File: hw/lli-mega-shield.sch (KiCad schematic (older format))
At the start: 6 parts

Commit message: Some schematics
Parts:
- added C? (x2): 1uF, symbol C
- added R? (x2): 75, symbol R
- added U? (x4): LM35, symbol LM35
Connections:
- wire segments 12 -> 26
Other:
- note added: "Battery Sensor"
- note added: "Temperature Sensors"
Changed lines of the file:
@@
-EESchema Schematic File Version 2  date fre 07 sep 2012 19:08:03 CEST
+EESchema Schematic File Version 2  date fre 07 sep 2012 20:49:57 CEST
 LIBS:power
 LIBS:device
@@
 Comment4 ""
 $EndDescr
+Text Notes 3300 4800 0    60   Italic 12
+Battery Sensor
+Text Notes 900  2800 0    60   Italic 12
+Temperature Sensors
+$Comp
+L LM35 U?
+U 1 1 504A41AE
+P 1500 4500
+F 0 "U?" H 1500 4650 60  0000 C CNN
+F 1 "LM35" H 1650 4250 60  0000 C CNN
+	1    1500 4500
+	1    0    0    -1
+$EndComp
+$Comp
+L R R?
+U 1 1 504A41AD
+P 2150 4800
+F 0 "R?" V 2230 4800 50  0000 C CNN
+F 1 "75" V 2150 4800 50  0000 C CNN
+	1    2150 4800
+	1    0    0    -1
+$EndComp
+$Comp
+L C C?
+U 1 1 504A41AC
+P 2150 5300
+F 0 "C?" H 2200 5400 50  0000 L CNN
+F 1 "1uF" H 2200 5200 50  0000 L CNN
+	1    2150 5300
+	1    0    0    -1
+$EndComp
+$Comp
+L GND #PWR?
+U 1 1 504A41AB
+P 1500 5100
+F 0 "#PWR?" H 1500 5100 30  0001 C CNN
+F 1 "GND" H 1500 5030 30  0001 C CNN
+	1    1500 5100
+	1    0    0    -1
+$EndComp
+$Comp
+L +5V #PWR?
+U 1 1 504A41AA
+P 900 4450
+F 0 "#PWR?" H 900 4540 20  0001 C CNN
+F 1 "+5V" H 900 4540 30  0000 C CNN
+	1    900  4450
+	1    0    0    -1
+$EndComp
+$Comp
+L LM35 U?
+U 1 1 504A41A9
+P 1500 4500
+F 0 "U?" H 1500 4650 60  0000 C CNN
+F 1 "LM35" H 1650 4250 60  0000 C CNN
+	1    1500 4500
+	1    0    0    -1
+$EndComp
+$Comp
+L GND #PWR?
+U 1 1 504A41A8
+P 2150 5550
+F 0 "#PWR?" H 2150 5550 30  0001 C CNN
+F 1 "GND" H 2150 5480 30  0001 C CNN
+	1    2150 5550
+	1    0    0    -1
+$EndComp
+Wire Wire Line
+	900  4500 950  4500
+Wire Wire Line
+	900  4450 900  4500
+Wire Wire Line
+	2200 4500 2050 4500
+Wire Wire Line
+	2150 5100 2150 5050
+Wire Wire Line
+	2150 4500 2150 4550
+Connection ~ 2150 4500
+Wire Wire Line
+	1500 5100 1500 5000
+Wire Wire Line
+	2150 5550 2150 5500
+Wire Wire Line
+	2150 4200 2150 4150
+Wire Wire Line
+	1500 3750 1500 3650
+Connection ~ 2150 3150
+Wire Wire Line
+	2150 3150 2150 3200
+Wire Wire Line
+	2150 3750 2150 3700
+Wire Wire Line
+	1450 7200 1450 7150
+Wire Wire Line
+	1450 6450 1450 6750
+Wire Wire Line
+	1450 6450 1500 6450
+Wire Wire Line
+	1850 1000 1600 1000
+Wire Wire Line
+	1800 1300 1600 1300
+Wire Wire Line
+	1600 1600 1700 1600
+Wire Wire Line
+	1700 1600 1700 1650
+Wire Wire Line
+	1600 1500 1700 1500
+Wire Wire Line
+	1600 1200 1800 1200
+Wire Notes Line
+	1950 1750 1950 700
+Wire Notes Line
+	1950 1750 650  1750
+Wire Notes Line
+	650  1750 650  700
+Wire Notes Line
+	650  700  1950 700
+Wire Wire Line
+	1150 6350 1500 6350
+Connection ~ 1300 6350
+Wire Wire Line
+	1450 6750 1300 6750
+Wire Wire Line
+	1750 6950 1800 6950
+Wire Wire Line
+	2200 3150 2050 3150
+Wire Wire Line
+	900  3100 900  3150
+Wire Wire Line
+	900  3150 950  3150
+$Comp
+L GND #PWR?
+U 1 1 504A414B
+P 2150 4200
+F 0 "#PWR?" H 2150 4200 30  0001 C CNN
+F 1 "GND" H 2150 4130 30  0001 C CNN
+	1    2150 4200
+	1    0    0    -1
+$EndComp
+$Comp
+L LM35 U?
+U 1 1 504A39E8
+P 1500 3150
+F 0 "U?" H 1500 3300 60  0000 C CNN
+F 1 "LM35" H 1650 2900 60  0000 C CNN
+	1    1500 3150
+	1    0    0    -1
+$EndComp
+$Comp
+L +5V #PWR?
+U 1 1 504A39DE
+P 900 3100
+F 0 "#PWR?" H 900 3190 20  0001 C CNN
+F 1 "+5V" H 900 3190 30  0000 C CNN
+	1    900  3100
+	1    0    0    -1
+$EndComp
+$Comp
+L GND #PWR?
+U 1 1 504A39D5
+P 1500 3750
+F 0 "#PWR?" H 1500 3750 30  0001 C CNN
+F 1 "GND" H 1500 3680 30  0001 C CNN
+	1    1500 3750
+	1    0    0    -1
+$EndComp
+$Comp
+L C C?
+U 1 1 504A39C7
+P 2150 3950
+F 0 "C?" H 2200 4050 50  0000 L CNN
+F 1 "1uF" H 2200 3850 50  0000 L CNN
+	1    2150 3950
+	1    0    0    -1
+$EndComp
+$Comp
+L R R?
+U 1 1 504A39C1
+P 2150 3450
+F 0 "R?" V 2230 3450 50  0000 C CNN
+F 1 "75" V 2150 3450 50  0000 C CNN
+	1    2150 3450
+	1    0    0    -1
+$EndComp
+$Comp
+L LM35 U?
+U 1 1 504A39B9
+P 1500 3150
+F 0 "U?" H 1500 3300 60  0000 C CNN
+F 1 "LM35" H 1650 2900 60  0000 C CNN
+	1    1500 3150
+	1    0    0    -1
+$EndComp
 Text Notes 1000 7400 0    60   ~ 0
 Disconnects supply to all actuators
@@
 $EndComp
 NoConn ~ 2300 6050
-Wire Wire Line
-	1750 6950 1800 6950
-Wire Wire Line
-	1300 6750 1450 6750
-Connection ~ 1300 6350
-Wire Wire Line
-	1150 6350 1500 6350
-Wire Notes Line
-	650  700  1950 700
-Wire Notes Line
-	650  700  650  1750
-Wire Notes Line
-	650  1750 1950 1750
-Wire Notes Line
-	1950 1750 1950 700
-Wire Wire Line
-	1600 1200 1800 1200
-Wire Wire Line
-	1600 1500 1700 1500
-Wire Wire Line
-	1700 1650 1700 1600
-Wire Wire Line
-	1700 1600 1600 1600
-Wire Wire Line
-	1800 1300 1600 1300
-Wire Wire Line
-	1850 1000 1600 1000
-Wire Wire Line
-	1500 6450 1450 6450
-Wire Wire Line
-	1450 6450 1450 6750
-Wire Wire Line
-	1450 7200 1450 7150
 $Comp
 L R R?

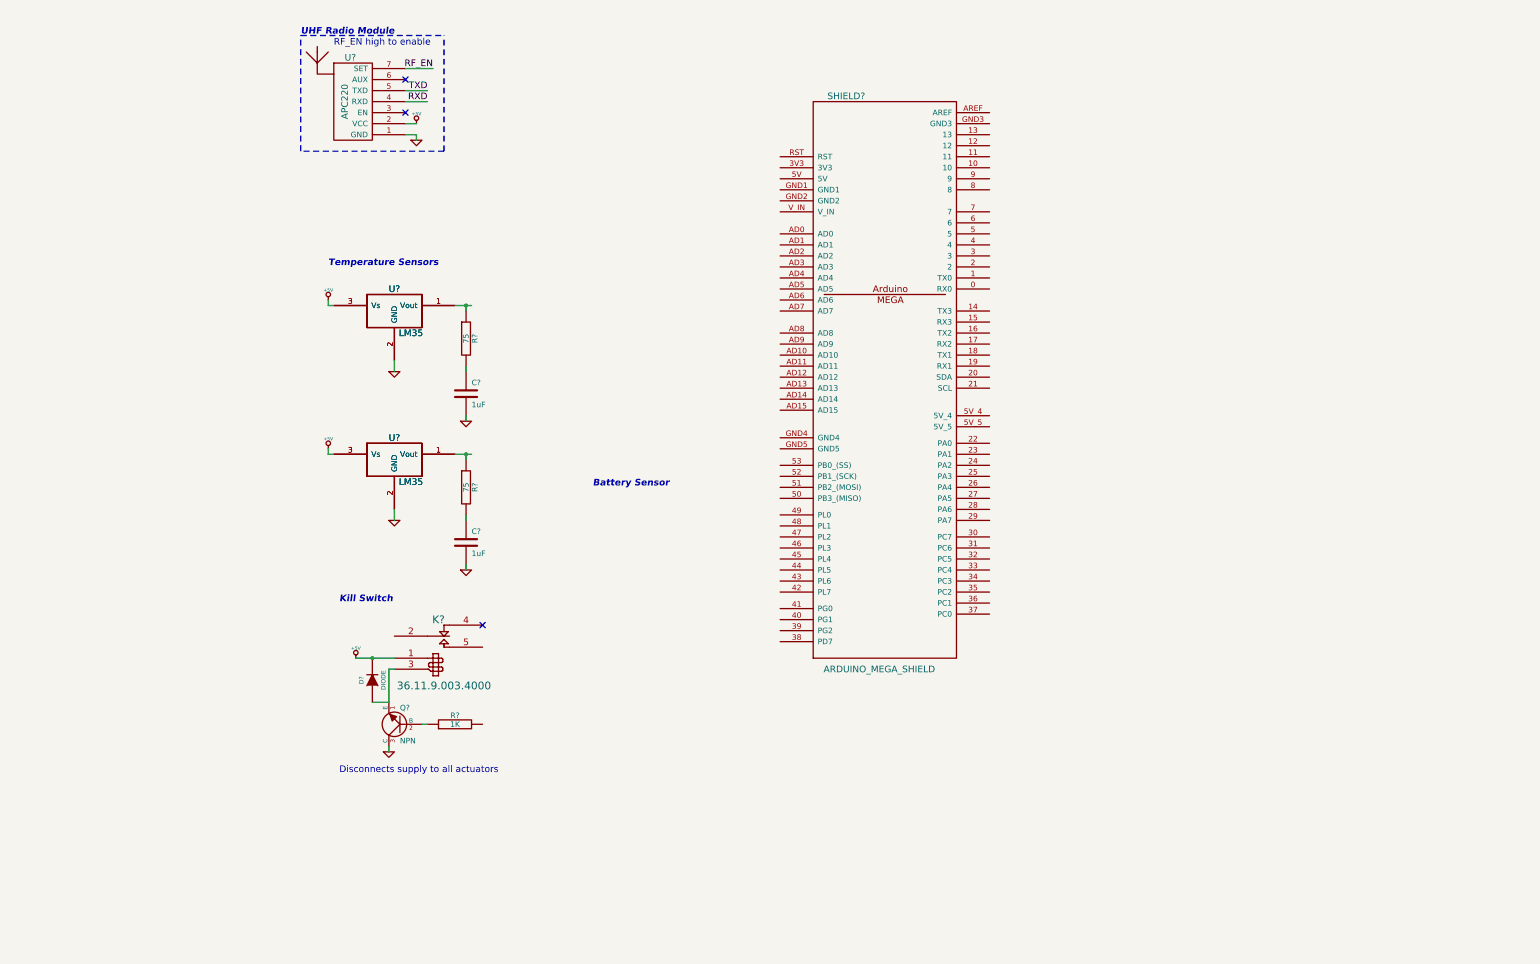
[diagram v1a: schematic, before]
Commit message: Added some more periphals on the hardware schematic
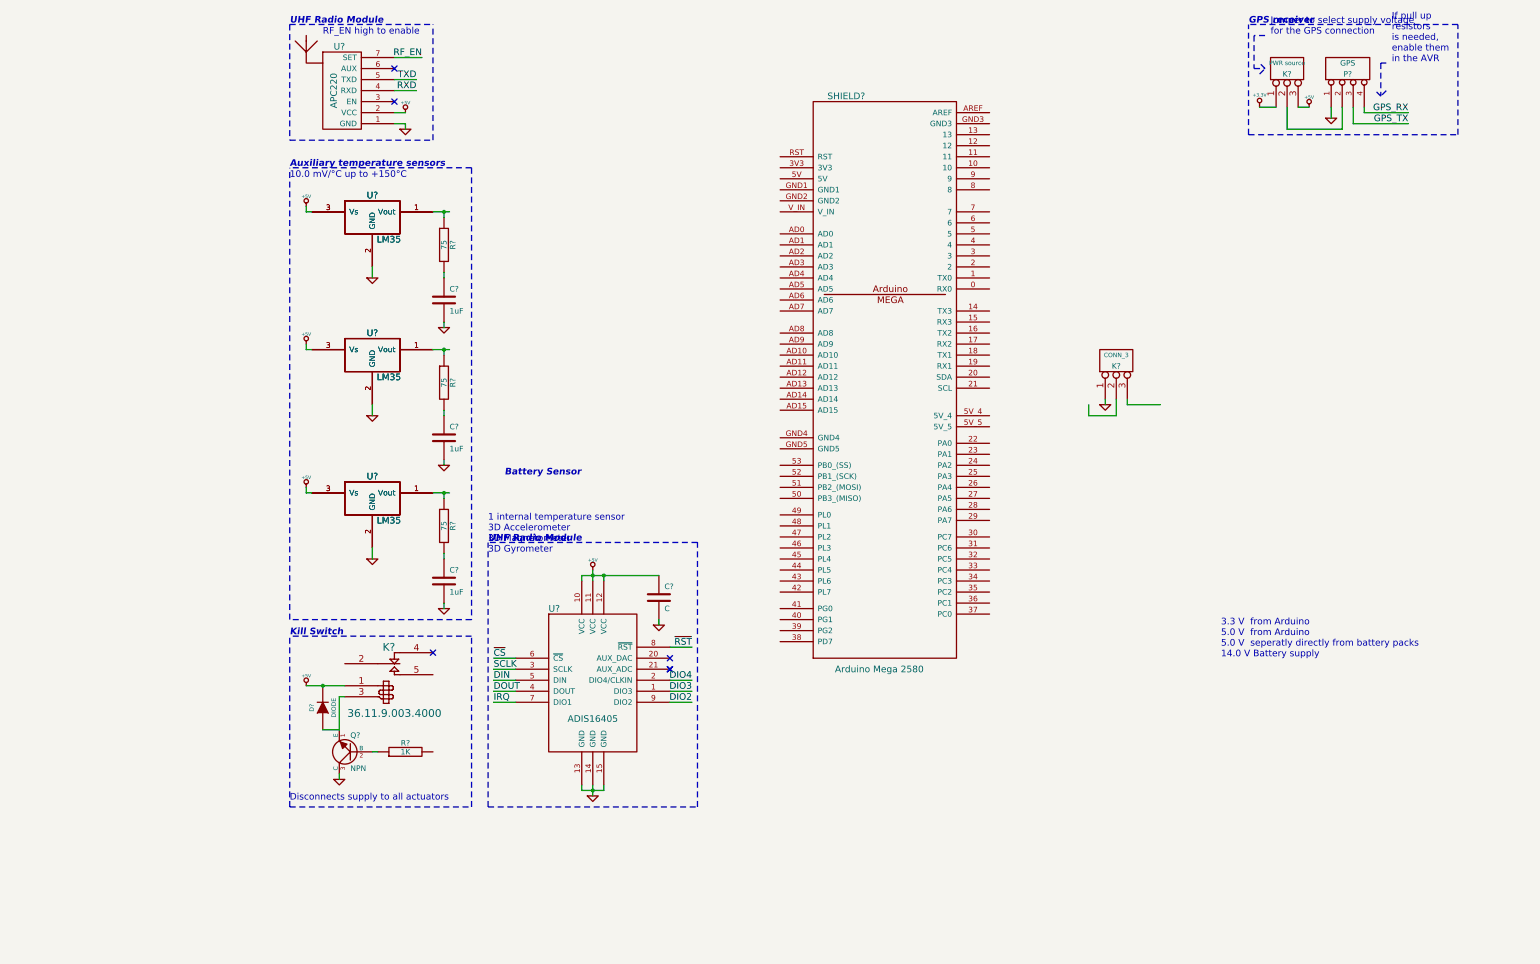
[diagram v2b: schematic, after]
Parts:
- added C?: C, symbol C
- added C?: 1uF, symbol C
- added K?: PWR source, symbol CONN_3
- added K?: CONN_3, symbol CONN_3
- added P?: GPS, symbol CONN_4
- added R?: 75, symbol R
- added U?: ADIS16405, symbol ADIS16405
- added U? (x2): LM35, symbol LM35
- SHIELD?: value ARDUINO_MEGA_SHIELD -> Arduino Mega 2580
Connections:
- net labels added: +3.3V, DIN, DIO2, DIO3, DIO4, DOUT, GPS_RX, GPS_TX, IRQ, SCLK, ~CS, ~RST
- wire segments 26 -> 67
- no-connect marks 3 -> 6
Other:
- note added: "1 internal temperature sensor\n3D Accelerometer\n3D Magnetometer\n3D Gyrometer"
- note added: "10.0 mV/°C up to +150°C"
- note added: "3.3 V from Arduino\n5.0 V from Arduino\n5.0 V seperatly directly from battery packs\n14.0 V Battery supply"
- note added: "Auxiliary temperature sensors"
- note added: "GPS receiver"
- note added: "If pull up\nresistors\nis needed,\nenable them\nin the AVR"
- note added: "Jumper to select supply voltage\nfor the GPS connection"
- note removed: "Temperature Sensors"
- moved on the sheet: C?, D?, K?, Q?, R?, U?

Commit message: Added more electronics
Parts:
- added D? (x2): LED, symbol LED
- added K?: AC1, symbol CONN_3
- added K?: AC3, symbol CONN_3
- added R? (x2): R, symbol R
- added U?: R-78B-1.5, symbol 7805
- K?: value CONN_3 -> AC2
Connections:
- net labels added: +BATT, AC1, AC2, AC3, LED1, LED2, LLH_RX, LLH_TX, RF_RX, RF_TX
- net labels removed: RXD, TXD
- wire segments 67 -> 118
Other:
- note added: "3.3 V from Arduino\n 5.0 V from Arduino\n 5.0 V seperatly directly from battery packs\n14.4 V battery supply"
- note added: "Blinkenlights"
- note added: "IMU"
- note added: "PWM controlled actuators"
- note added: "Switching Regulator,\n6.5-18Vin,5Vout 1.5A"
- note added: "This should probably be\nseperated from the arduino\n5V regulator"
- note removed: "3.3 V from Arduino\n5.0 V from Arduino\n5.0 V seperatly directly from battery packs\n14.0 V Battery supply"
- moved on the sheet: K?, P?

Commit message: More hardware before I go home
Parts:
- D?: value DIODE -> 1N4148
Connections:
- net ~KILL: now reaches R?.2
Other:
- moved on the sheet: U?

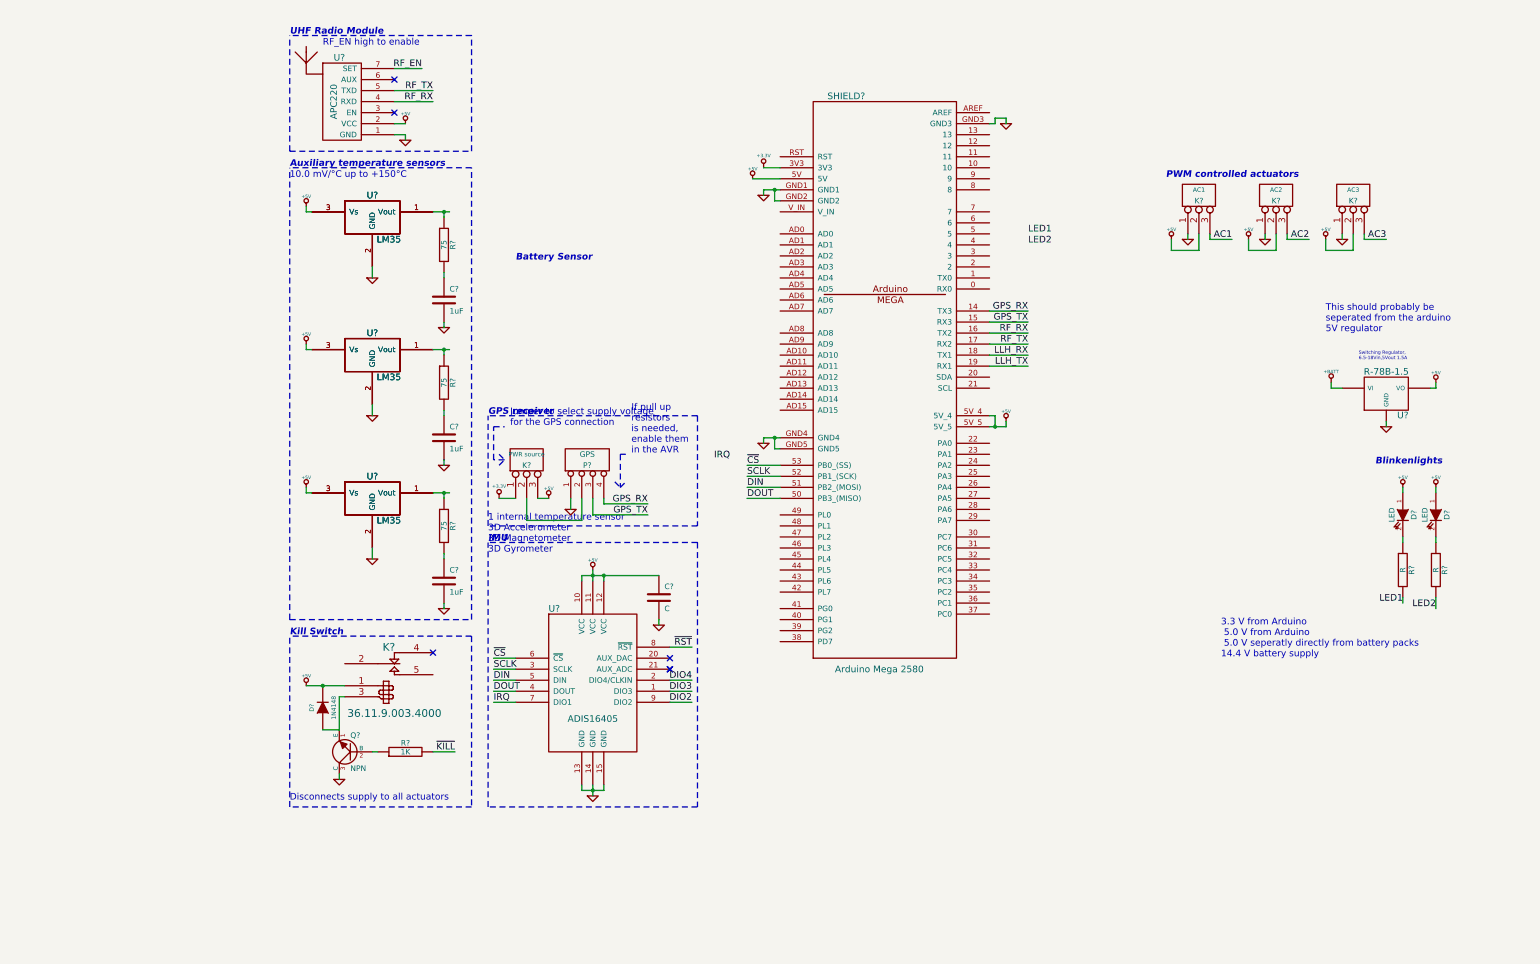
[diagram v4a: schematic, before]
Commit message: Added a quadrature encoder input
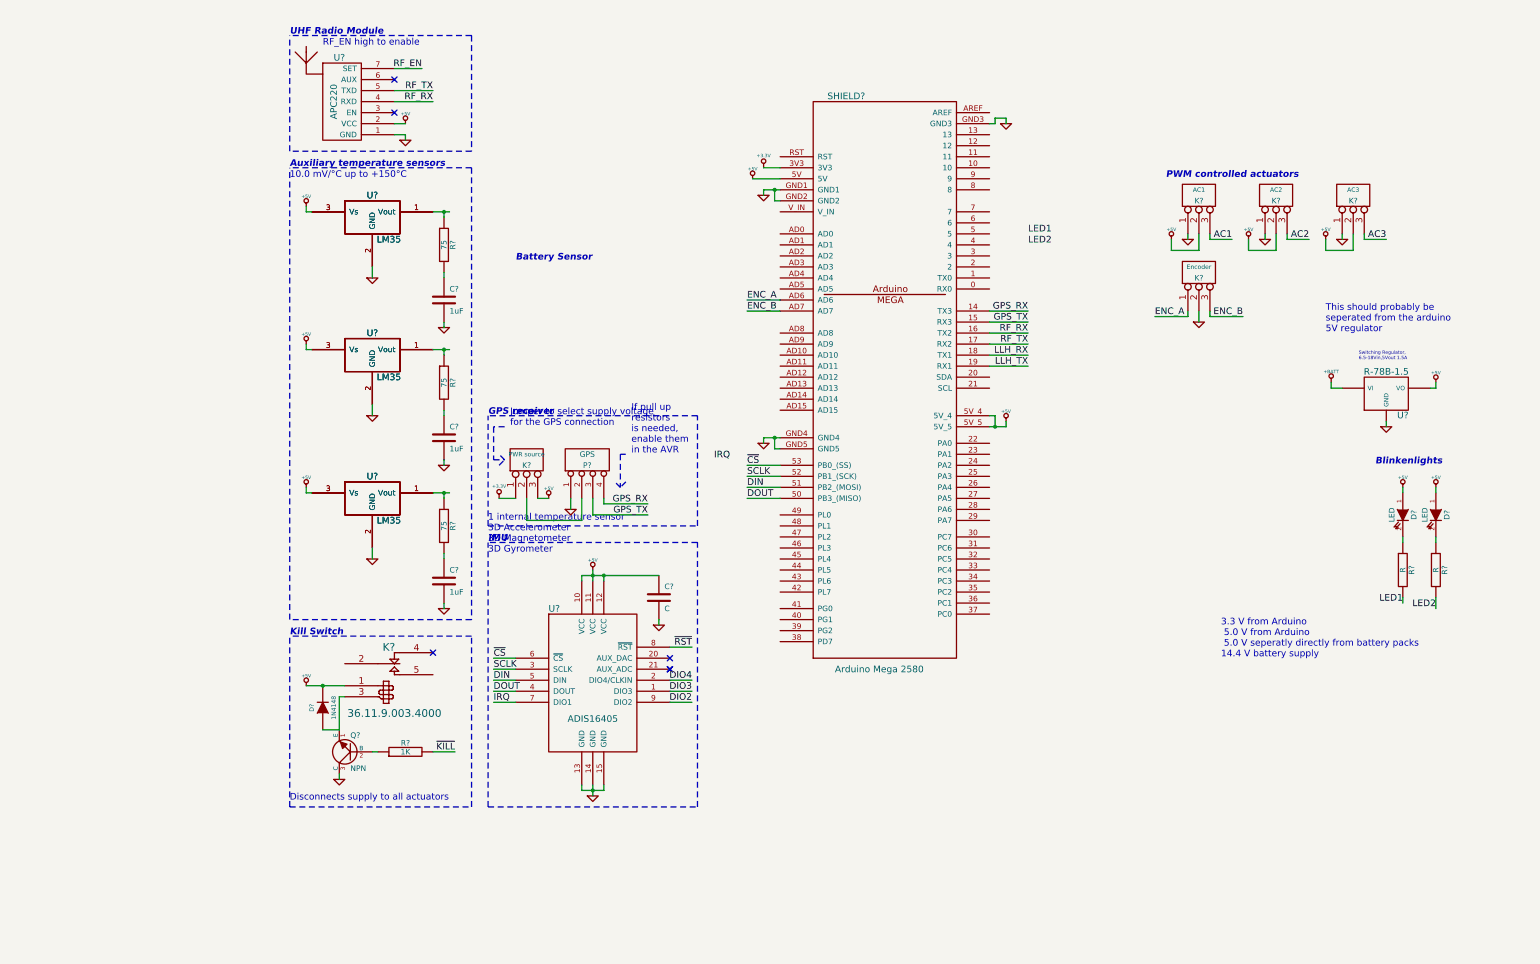
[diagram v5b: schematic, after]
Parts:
- added K?: Encoder, symbol CONN_3
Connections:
- net GND: now also K?.2 (PM)
- net ENC_A: now reaches SHIELD?.AD6
- net ENC_A: now also K?.1 (P1)
- net ENC_B: now reaches SHIELD?.AD7
- net ENC_B: now also K?.3 (P3)
